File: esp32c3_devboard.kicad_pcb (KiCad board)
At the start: 4 copper layers, 47 x 34 mm, 72 parts, among them J1 USB_C_Receptacle_USB2.0, J2 Conn_01x15_Male, J3 Conn_01x15_Male, Q1 S8050, Q2 S8050, U1 AMS1117-3.3, U2 SRV05-4, U3 USB2514B_Bi, U4 CP2102N-A01-GQFN28, U5 ESP32-C3-WROOM-02-SOCKET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

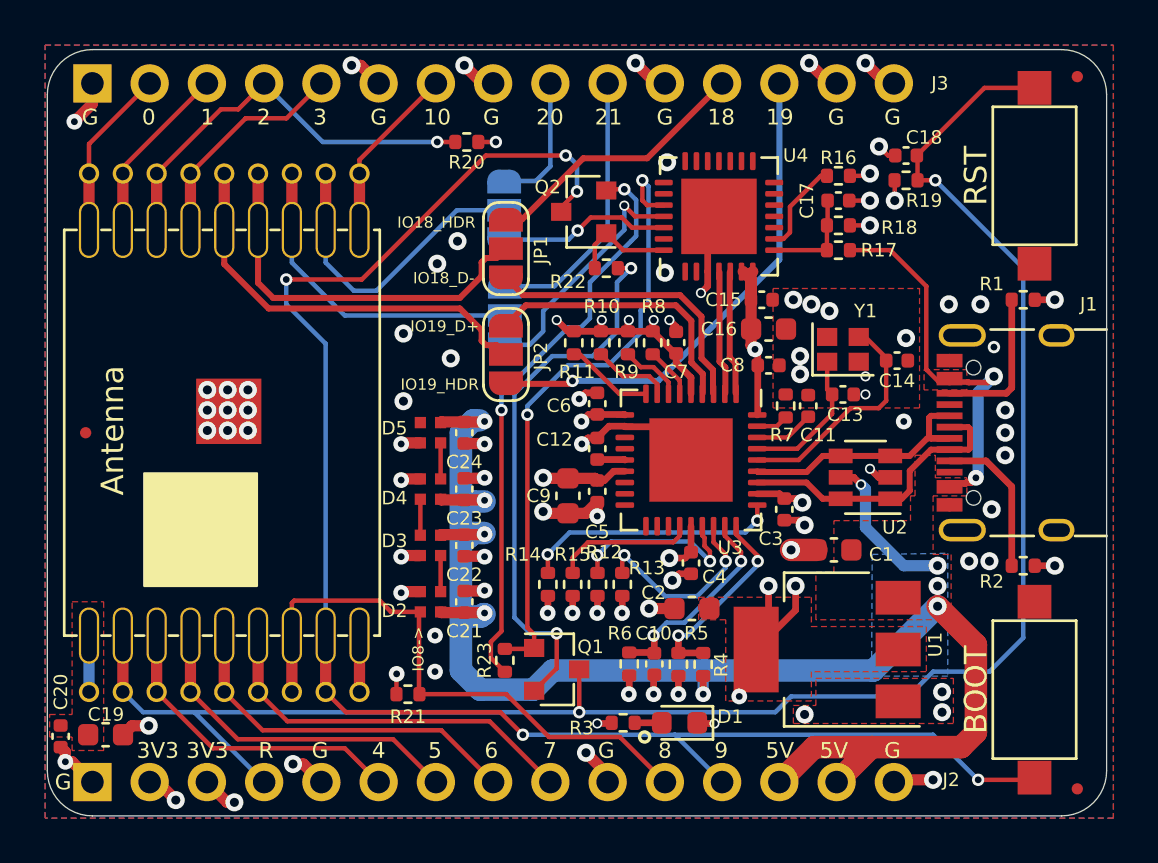
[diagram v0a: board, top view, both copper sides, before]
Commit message: Update project to KiCAD v6, fix BJT wrong symbol pinout
Signed-off-by: Tomislav Milkovic <tomislav.milkovic95@gmail.com>
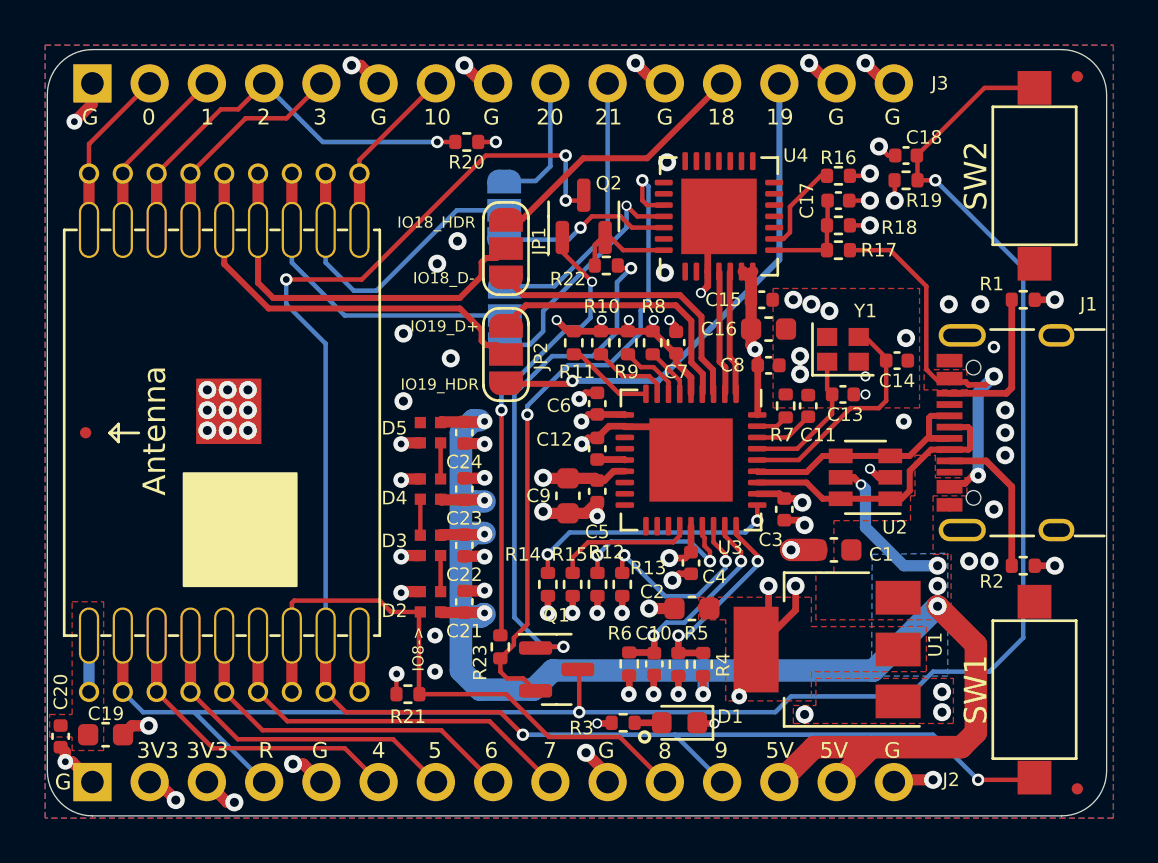
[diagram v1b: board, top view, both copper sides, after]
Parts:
- U5: footprint Espressif custom:ESP32-C3-WROOM-02-SOCKET -> Espressif_custom:ESP32-C3-WROOM-02-SOCKET
- moved R23 0.63 mm to (134.8, 107.7), turned to -90 degrees
- moved Q2 0.20 mm to (138.5, 88.6), turned to 90 degrees
- moved R22 0.12 mm to (139.5, 90.8)
- renumbered BOOT to SW1, RST to SW2
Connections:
- net +3V3 renamed +3.3V
- net /ESP32-C3 module/~RST renamed /ESP32-C3 module/~{RST}
- net /USB hub/DOWNSTREAM_USB2_D+ renamed /ESP32-C3 module/ESP32_USB_D+
- net /USB hub/DOWNSTREAM_USB2_D- renamed /ESP32-C3 module/ESP32_USB_D-
- D5 pad 2: (no net) -> unconnected-(D5-Pad2)
- J1 pad A8: (no net) -> unconnected-(J1-PadA8)
- J1 pad B8: (no net) -> unconnected-(J1-PadB8)
- J1 pad S1: Net-(J1-PadS1) -> unconnected-(J1-PadS1)
- Q1 pad 1: /ESP32-C3 module/ESP32_UART_RTS -> Net-(Q1-Pad1)
- Q1 pad 2: Net-(Q1-Pad2) -> /ESP32-C3 module/ESP32_UART_RTS
- Q2 pad 1: /ESP32-C3 module/ESP32_UART_DTR -> Net-(Q2-Pad1)
- Q2 pad 2: Net-(Q2-Pad2) -> /ESP32-C3 module/ESP32_UART_DTR
- R22 pad 1: Net-(Q1-Pad2) -> Net-(Q1-Pad1)
- R23 pad 1: Net-(Q2-Pad2) -> Net-(Q2-Pad1)
- U3 pad 12: (no net) -> unconnected-(U3-Pad12)
- U3 pad 13: (no net) -> unconnected-(U3-Pad13)
- U3 pad 16: (no net) -> unconnected-(U3-Pad16)
- U3 pad 17: (no net) -> unconnected-(U3-Pad17)
- U3 pad 18: (no net) -> unconnected-(U3-Pad18)
- U3 pad 19: (no net) -> unconnected-(U3-Pad19)
- U3 pad 20: (no net) -> unconnected-(U3-Pad20)
- U3 pad 21: (no net) -> unconnected-(U3-Pad21)
- U4 pad 1: (no net) -> unconnected-(U4-Pad1)
- U4 pad 10: (no net) -> unconnected-(U4-Pad10)
- U4 pad 11: (no net) -> unconnected-(U4-Pad11)
- U4 pad 12: (no net) -> unconnected-(U4-Pad12)
- U4 pad 13: (no net) -> unconnected-(U4-Pad13)
- U4 pad 14: (no net) -> unconnected-(U4-Pad14)
- U4 pad 15: (no net) -> unconnected-(U4-Pad15)
- U4 pad 16: (no net) -> unconnected-(U4-Pad16)
- U4 pad 17: (no net) -> unconnected-(U4-Pad17)
- U4 pad 18: (no net) -> unconnected-(U4-Pad18)
- U4 pad 19: (no net) -> unconnected-(U4-Pad19)
- U4 pad 2: (no net) -> unconnected-(U4-Pad2)
- U4 pad 20: (no net) -> unconnected-(U4-Pad20)
- U4 pad 21: (no net) -> unconnected-(U4-Pad21)
- U4 pad 22: (no net) -> unconnected-(U4-Pad22)
- U4 pad 23: (no net) -> unconnected-(U4-Pad23)
- U4 pad 27: (no net) -> unconnected-(U4-Pad27)
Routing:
- net Net-(Q2-Pad2): track 25.7 -> 0.00 mm, vias 2 -> 0
- net Net-(Q1-Pad2): track 24.4 -> 0.00 mm, vias 2 -> 0
- net Net-(Q1-Pad1): track 0.00 -> 23.2 mm, vias 0 -> 2
- net Net-(Q2-Pad1): track 0.00 -> 20.2 mm, vias 0 -> 2
- net /ESP32-C3 module/ESP32_UART_RTS: track 27.5 -> 29.2 mm
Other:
- net class Default removed
- net class USB removed
